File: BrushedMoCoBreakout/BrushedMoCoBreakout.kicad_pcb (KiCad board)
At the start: 2 copper layers, 61 x 35.6 mm, 19 parts, among them U1 DRV8244S

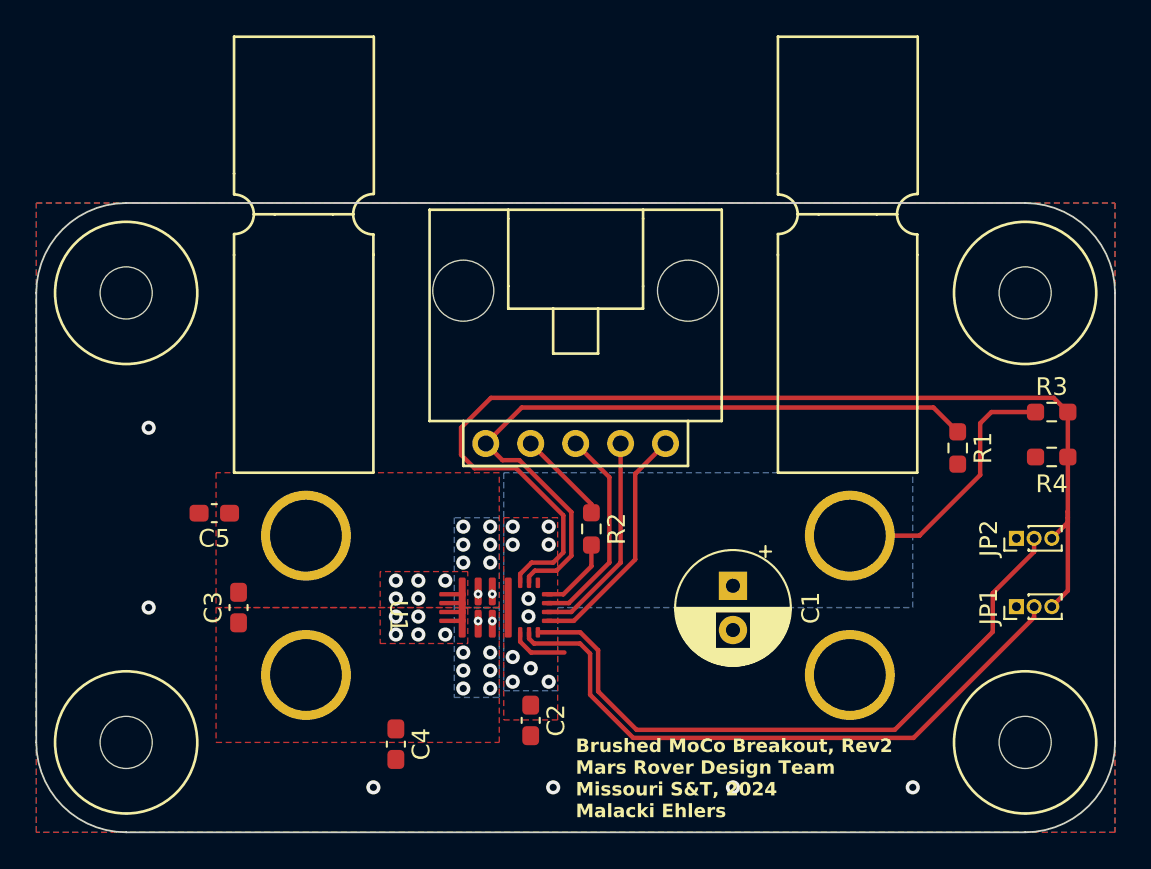
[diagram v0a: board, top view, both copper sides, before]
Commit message: Swap to square andersons
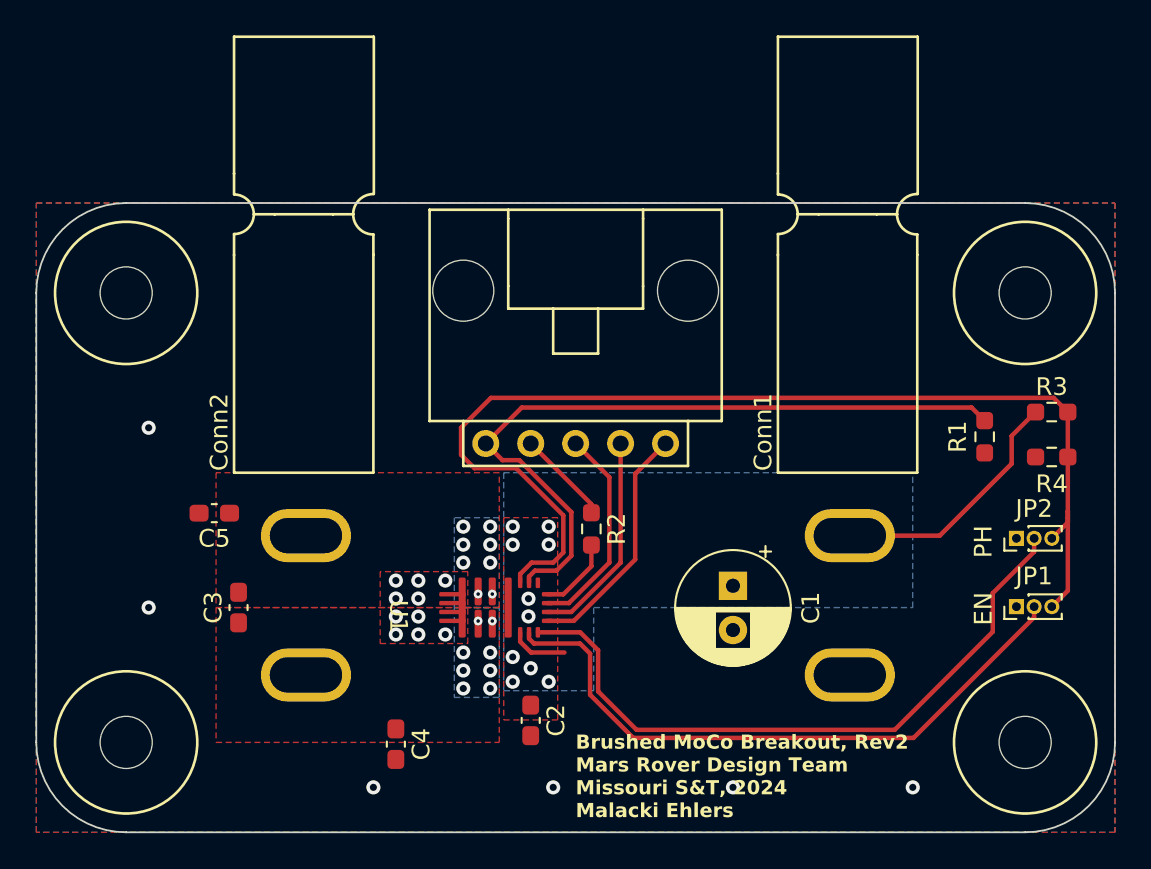
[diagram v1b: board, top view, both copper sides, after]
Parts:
- Conn1, Conn2: footprint MRDT_Connectors:Anderson_2_Horizontal_Stacked_PV -> MRDT_Connectors:Square_Anderson_2_H_Stacked_PV
- moved R1 1.65 mm to (105.7, 41.1)
- moved Conn1 0.57 mm to (98.4, 47.2)
- moved Conn2 0.57 mm to (67.7, 47.2)
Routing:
- net I_SENSE: track 40.2 -> 41.5 mm
- net +12V: track 15.1 -> 14.3 mm
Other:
- board text added: "EN"
- board text added: "PH"

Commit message: Adjust resistor values
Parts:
- R3: value 470k -> 47k
- R4: value 330k -> 33k
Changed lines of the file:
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@@
         (effects (font (size 1 1) (thickness 0.15)))
     )
-    (fp_text value "470k" (at 0 1.43) (layer "F.Fab")
+    (fp_text value "47k" (at 0 1.43) (layer "F.Fab")
         (effects (font (size 1 1) (thickness 0.15)))
     )
@@
         (effects (font (size 1 1) (thickness 0.15)))
     )
-    (fp_text value "330k" (at 0 -1.524) (layer "F.Fab")
+    (fp_text value "33k" (at 0 -1.524) (layer "F.Fab")
         (effects (font (size 1 1) (thickness 0.15)))
     )

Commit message: Add signature
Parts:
- added G***: LOGO, Signatures:Malacki_Ehlers_Signature, F.Cu at (55.1, 45.7)
